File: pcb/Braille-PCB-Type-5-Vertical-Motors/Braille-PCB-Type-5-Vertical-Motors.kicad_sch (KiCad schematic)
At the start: 39 parts, among them J1 Screw_Terminal_01x02, J2 Screw_Terminal_01x02, J21 Conn_01x05, J22 Conn_01x05, J23 Conn_01x05, J24 Conn_01x05, J3 Screw_Terminal_01x02, J4 Conn_01x03, J5 Conn_01x02, J6 Conn_01x08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

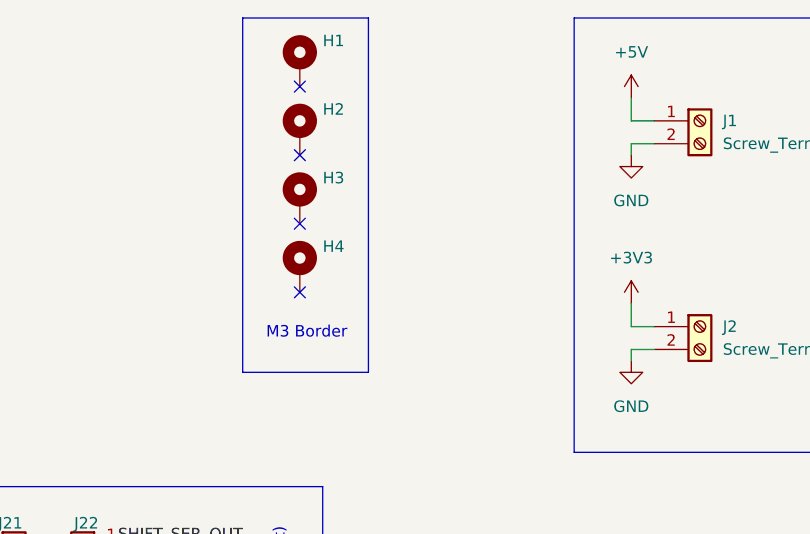
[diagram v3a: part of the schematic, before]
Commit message: PCB: Finish setting up power planes
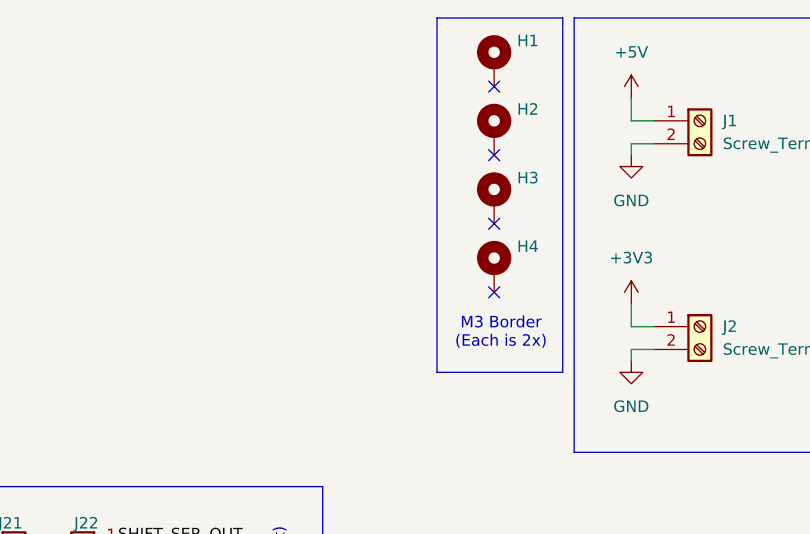
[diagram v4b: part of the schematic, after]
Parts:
- H1, H2, H3, H4: footprint MountingHole:MountingHole_3.2mm_M3_Pad -> 00-project-footprints:MountingHole_M3_2x_3mm_Pitch
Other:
- note added: "M3 Border (Each is 2x)"
- note removed: "M3 Border"
- moved on the sheet: H1, H2, H3, H4
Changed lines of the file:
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@@
 	)
 	(no_connect
-		(at 191.77 29.21)
+		(at 213.36 29.21)
 	)
 	(no_connect
-		(at 191.77 21.59)
+		(at 213.36 21.59)
 	)
 	(no_connect
@@
 	)
 	(no_connect
-		(at 191.77 36.83)
+		(at 213.36 36.83)
 	)
 	(no_connect
@@
 	)
 	(no_connect
-		(at 191.77 44.45)
+		(at 213.36 44.45)
 	)
 	(no_connect
@@
 	)
 	(rectangle
-		(start 185.42 13.97)
-		(end 199.39 53.34)
+		(start 207.01 13.97)
+		(end 220.98 53.34)
 		(stroke
 			(width 0)
@@
 		)
 	)
-	(text "M3 Border"
+	(text "M3 Border\n(Each is 2x)"
 		(exclude_from_sim no)
-		(at 192.532 49.022 0)
+		(at 214.122 49.022 0)
 		(effects
 			(font
@@
 	(symbol
 		(lib_id "Mechanical:MountingHole_Pad")
-		(at 191.77 41.91 0)
+		(at 213.36 41.91 0)
 		(unit 1)
 		(exclude_from_sim yes)
@@
 		(fields_autoplaced yes)
 		(property "Reference" "H4"
-			(at 194.31 39.3699 0)
+			(at 215.9 39.3699 0)
 			(effects
 				(font
@@
 		)
 		(property "Value" "MountingHole_Pad"
-			(at 194.31 41.9099 0)
+			(at 215.9 41.9099 0)
 			(effects
 				(font
@@
 			)
 		)
-		(property "Footprint" "MountingHole:MountingHole_3.2mm_M3_Pad"
-			(at 191.77 41.91 0)
+		(property "Footprint" "00-project-footprints:MountingHole_M3_2x_3mm_Pitch"
+			(at 213.36 41.91 0)
 			(effects
 				(font
@@
 		)
 		(property "Datasheet" "~"
-			(at 191.77 41.91 0)
+			(at 213.36 41.91 0)
 			(effects
 				(font
@@
 		)
 		(property "Description" "Mounting Hole with connection"
-			(at 191.77 41.91 0)
+			(at 213.36 41.91 0)
 			(effects
 				(font
@@
 	(symbol
 		(lib_id "Mechanical:MountingHole_Pad")
-		(at 191.77 19.05 0)
+		(at 213.36 19.05 0)
 		(unit 1)
 		(exclude_from_sim yes)
@@
 		(fields_autoplaced yes)
 		(property "Reference" "H1"
-			(at 194.31 16.5099 0)
+			(at 215.9 16.5099 0)
 			(effects
 				(font
@@
 		)
 		(property "Value" "MountingHole_Pad"
-			(at 194.31 19.0499 0)
+			(at 215.9 19.0499 0)
 			(effects
 				(font
@@
 			)
 		)
-		(property "Footprint" "MountingHole:MountingHole_3.2mm_M3_Pad"
-			(at 191.77 19.05 0)
+		(property "Footprint" "00-project-footprints:MountingHole_M3_2x_3mm_Pitch"
+			(at 213.36 19.05 0)
 			(effects
 				(font
@@
 		)
 		(property "Datasheet" "~"
-			(at 191.77 19.05 0)
+			(at 213.36 19.05 0)
 			(effects
 				(font
@@
 		)
 		(property "Description" "Mounting Hole with connection"
-			(at 191.77 19.05 0)
+			(at 213.36 19.05 0)
 			(effects
 				(font
@@
 	(symbol
 		(lib_id "Mechanical:MountingHole_Pad")
-		(at 191.77 26.67 0)
+		(at 213.36 26.67 0)
 		(unit 1)
 		(exclude_from_sim yes)
@@
 		(fields_autoplaced yes)
 		(property "Reference" "H2"
-			(at 194.31 24.1299 0)
+			(at 215.9 24.1299 0)
 			(effects
 				(font
@@
 		)
 		(property "Value" "MountingHole_Pad"
-			(at 194.31 26.6699 0)
+			(at 215.9 26.6699 0)
 			(effects
 				(font
@@
 			)
 		)
-		(property "Footprint" "MountingHole:MountingHole_3.2mm_M3_Pad"
-			(at 191.77 26.67 0)
+		(property "Footprint" "00-project-footprints:MountingHole_M3_2x_3mm_Pitch"
+			(at 213.36 26.67 0)
 			(effects
 				(font
@@
 		)
 		(property "Datasheet" "~"
-			(at 191.77 26.67 0)
+			(at 213.36 26.67 0)
 			(effects
 				(font
@@
 		)
 		(property "Description" "Mounting Hole with connection"
-			(at 191.77 26.67 0)
+			(at 213.36 26.67 0)
 			(effects
 				(font
@@
 	(symbol
 		(lib_id "Mechanical:MountingHole_Pad")
-		(at 191.77 34.29 0)
+		(at 213.36 34.29 0)
 		(unit 1)
 		(exclude_from_sim yes)
@@
 		(fields_autoplaced yes)
 		(property "Reference" "H3"
-			(at 194.31 31.7499 0)
+			(at 215.9 31.7499 0)
 			(effects
 				(font
@@
 		)
 		(property "Value" "MountingHole_Pad"
-			(at 194.31 34.2899 0)
+			(at 215.9 34.2899 0)
 			(effects
 				(font
@@
 			)
 		)
-		(property "Footprint" "MountingHole:MountingHole_3.2mm_M3_Pad"
-			(at 191.77 34.29 0)
+		(property "Footprint" "00-project-footprints:MountingHole_M3_2x_3mm_Pitch"
+			(at 213.36 34.29 0)
 			(effects
 				(font
@@
 		)
 		(property "Datasheet" "~"
-			(at 191.77 34.29 0)
+			(at 213.36 34.29 0)
 			(effects
 				(font
@@
 		)
 		(property "Description" "Mounting Hole with connection"
-			(at 191.77 34.29 0)
+			(at 213.36 34.29 0)
 			(effects
 				(font

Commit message: Finish Type 5 Rev 1 PCB
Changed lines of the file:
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@@
 	(paper "USLetter")
 	(title_block
-		(date "2024-11-27")
-		(rev "Rev 2")
+		(date "2025-01-10")
+		(rev "Type 5 Rev 1")
 	)
 	(junction
@@
 	)
 	(junction
-		(at 174.625 99.06)
+		(at 175.26 88.9)
 		(diameter 0)
 		(color 0 0 0 0)
 	)
 	(junction
-		(at 53.34 151.13)
+		(at 175.26 96.52)
 		(diameter 0)
 		(color 0 0 0 0)
 	)
 	(junction
-		(at 44.45 146.05)
+		(at 175.26 99.06)
 		(diameter 0)
 		(color 0 0 0 0)
 	)
 	(junction
-		(at 152.4 88.9)
+		(at 53.34 151.13)
 		(diameter 0)
 		(color 0 0 0 0)
 	)
 	(junction
-		(at 33.02 173.99)
+		(at 44.45 146.05)
 		(diameter 0)
 		(color 0 0 0 0)
 	)
 	(junction
-		(at 41.91 163.83)
+		(at 152.4 88.9)
 		(diameter 0)
 		(color 0 0 0 0)
 	)
 	(junction
-		(at 174.625 88.9)
+		(at 33.02 173.99)
 		(diameter 0)
 		(color 0 0 0 0)
 	)
 	(junction
-		(at 152.4 99.06)
+		(at 41.91 163.83)
 		(diameter 0)
 		(color 0 0 0 0)
 	)
 	(junction
-		(at 46.99 151.13)
+		(at 152.4 99.06)
 		(diameter 0)
 		(color 0 0 0 0)
 	)
 	(junction
-		(at 174.625 96.52)
+		(at 46.99 151.13)
 		(diameter 0)
 		(color 0 0 0 0)
@@
 	(wire
 		(pts
-			(xy 174.625 99.06) (xy 172.72 99.06)
+			(xy 172.72 99.06) (xy 175.26 99.06)
 		)
 		(stroke
@@
 	(wire
 		(pts
-			(xy 174.625 88.9) (xy 175.895 88.9)
-		)
-		(stroke
-			(width 0)
-			(type default)
-		)
-	)
-	(wire
-		(pts
 			(xy 20.32 104.14) (xy 20.32 107.95)
 		)
@@
 	(wire
 		(pts
-			(xy 174.625 96.52) (xy 172.72 96.52)
+			(xy 172.72 96.52) (xy 175.26 96.52)
 		)
 		(stroke
@@
 	(wire
 		(pts
-			(xy 174.625 88.9) (xy 172.72 88.9)
+			(xy 172.72 88.9) (xy 175.26 88.9)
 		)
 		(stroke
@@
 	(wire
 		(pts
+			(xy 175.26 88.9) (xy 177.8 88.9)
+		)
+		(stroke
+			(width 0)
+			(type default)
+		)
+	)
+	(wire
+		(pts
 			(xy 228.6 22.86) (xy 228.6 25.4)
 		)
@@
 	(wire
 		(pts
-			(xy 172.72 91.44) (xy 174.625 91.44)
+			(xy 172.72 91.44) (xy 175.26 91.44)
 		)
 		(stroke
@@
 	(wire
 		(pts
-			(xy 172.72 93.98) (xy 174.625 93.98)
+			(xy 172.72 93.98) (xy 175.26 93.98)
 		)
 		(stroke
@@
 	(wire
 		(pts
-			(xy 174.625 91.44) (xy 174.625 88.9)
+			(xy 175.26 91.44) (xy 175.26 88.9)
 		)
 		(stroke
@@
 	(wire
 		(pts
-			(xy 175.895 99.06) (xy 174.625 99.06)
+			(xy 177.8 99.06) (xy 175.26 99.06)
 		)
 		(stroke
@@
 	(wire
 		(pts
-			(xy 174.625 93.98) (xy 174.625 96.52)
+			(xy 175.26 93.98) (xy 175.26 96.52)
 		)
 		(stroke
@@
 	(wire
 		(pts
-			(xy 174.625 96.52) (xy 174.625 99.06)
+			(xy 175.26 96.52) (xy 175.26 99.06)
 		)
 		(stroke
@@
 	(symbol
 		(lib_id "power:VDC")
-		(at 175.895 88.9 270)
+		(at 177.8 88.9 270)
 		(mirror x)
 		(unit 1)
@@
 		(fields_autoplaced yes)
 		(property "Reference" "#PWR035"
-			(at 172.085 88.9 0)
+			(at 173.99 88.9 0)
 			(effects
 				(font
@@
 		)
 		(property "Value" "VDC"
-			(at 179.705 88.8999 90)
+			(at 181.61 88.8999 90)
 			(effects
 				(font
@@
 		)
 		(property "Footprint" ""
-			(at 175.895 88.9 0)
+			(at 177.8 88.9 0)
 			(effects
 				(font
@@
 		)
 		(property "Datasheet" ""
-			(at 175.895 88.9 0)
+			(at 177.8 88.9 0)
 			(effects
 				(font
@@
 		)
 		(property "Description" "Power symbol creates a global label with name \"VDC\""
-			(at 175.895 88.9 0)
+			(at 177.8 88.9 0)
 			(effects
 				(font
@@
 	(symbol
 		(lib_id "power:GND")
-		(at 175.895 99.06 90)
+		(at 177.8 99.06 90)
 		(mirror x)
 		(unit 1)
@@
 		(fields_autoplaced yes)
 		(property "Reference" "#PWR036"
-			(at 182.245 99.06 0)
+			(at 184.15 99.06 0)
 			(effects
 				(font
@@
 		)
 		(property "Value" "GND"
-			(at 179.705 99.0599 90)
+			(at 181.61 99.0599 90)
 			(effects
 				(font
@@
 		)
 		(property "Footprint" ""
-			(at 175.895 99.06 0)
+			(at 177.8 99.06 0)
 			(effects
 				(font
@@
 		)
 		(property "Datasheet" ""
-			(at 175.895 99.06 0)
+			(at 177.8 99.06 0)
 			(effects
 				(font
@@
 		)
 		(property "Description" "Power symbol creates a global label with name \"GND\" , ground"
-			(at 175.895 99.06 0)
+			(at 177.8 99.06 0)
 			(effects
 				(font
